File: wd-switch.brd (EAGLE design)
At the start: 40.3 x 59.7 mm, 18 parts, among them Q1 BC337, Q3 IRL540N, Q4 IRL540N, X1 KUSBVX

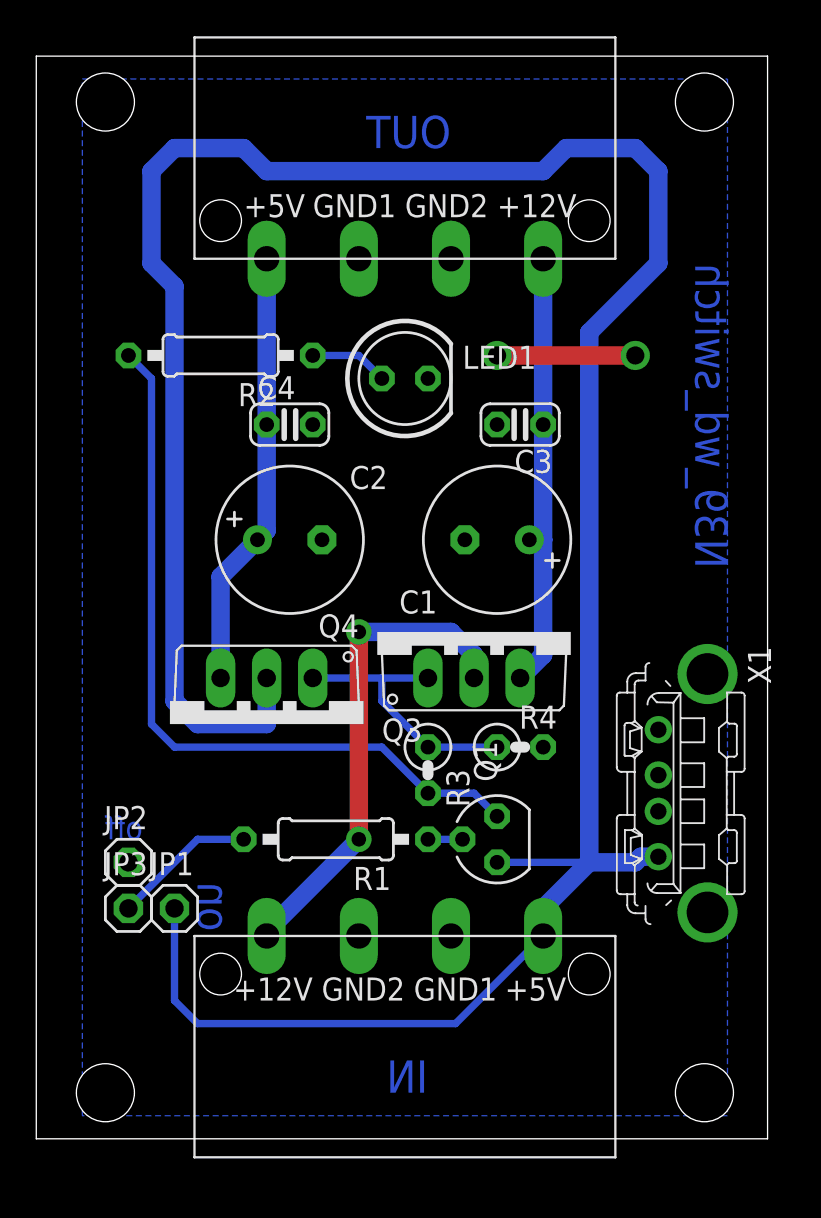
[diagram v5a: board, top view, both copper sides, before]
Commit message: WD-Switch jetzt mit Relais
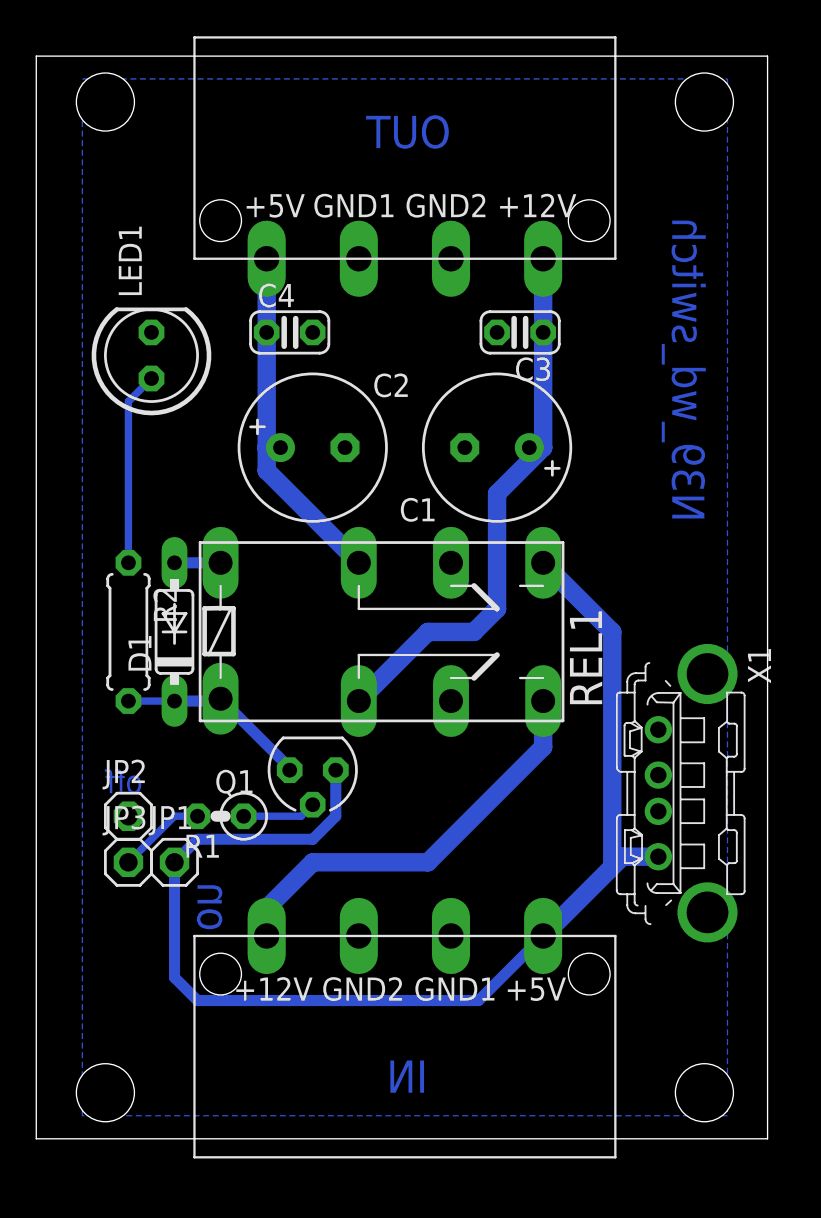
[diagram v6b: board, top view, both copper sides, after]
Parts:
- removed Q3, Q4: IRL540N, n39:TO220V
- removed R3: 100R, resistor:0207/2V
- removed R4: 100K, resistor:0207/2V
- added D1: 1N4148DO35-7, diode:DO35-7
- added REL1: RELAIS_2_WECHSLER, n39:RELAIS_DIL_M4
- R1: device resistor:0207/10 -> resistor:0207/2V
- R2: device resistor:0207/10 -> resistor:0207/7
- moved R2 16.1 mm to (5.08, 27.9), turned to 270 degrees
- moved LED1 14.0 mm to (6.35, 43.2), turned to 90 degrees
- moved Q1 10.9 mm to (15.2, 20.3), turned to 180 degrees
- moved R1 6.48 mm to (10.2, 17.8)
- moved C2 5.24 mm to (15.2, 38.1)
- moved C3 5.08 mm to (26.7, 44.5)
- moved C4 5.08 mm to (14.0, 44.5)
- moved C1 5.08 mm to (25.4, 38.1)
- moved JP1 2.54 mm to (7.62, 15.2)
- moved JP2 2.54 mm to (5.08, 17.8)
- moved JP3 2.54 mm to (5.08, 15.2)
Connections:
- removed net N$1: Q3.1, Q4.1, R3.1, R4.1
- net GND: now also D1.A, REL1.2; no longer R4.2
- net N$11: now also D1.C, REL1.1; no longer R3.2
- net N$2: now also REL1.P0; no longer Q3.3
- net N$4: now also REL1.P1; no longer Q4.3
- net VCC: now also REL1.S1; no longer Q4.2
- net VDD: now also REL1.S0; no longer Q3.2
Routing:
- net VCC: track 149.7 -> 67.4 mm
- net N$11: track 42.0 -> 10.6 mm
- net N$1: track 15.0 -> 0.00 mm
- net N$2: track 24.4 -> 30.8 mm
- net N$7: track 4.34 -> 10.7 mm
- net GND: track 7.62 -> 2.54 mm, vias 2 -> 0
- net N$4: track 24.2 -> 19.6 mm
- net VDD: track 27.0 -> 23.0 mm, vias 2 -> 0
- net N$5: track 7.93 -> 4.86 mm
- net N$3: track 1.91 -> 4.07 mm

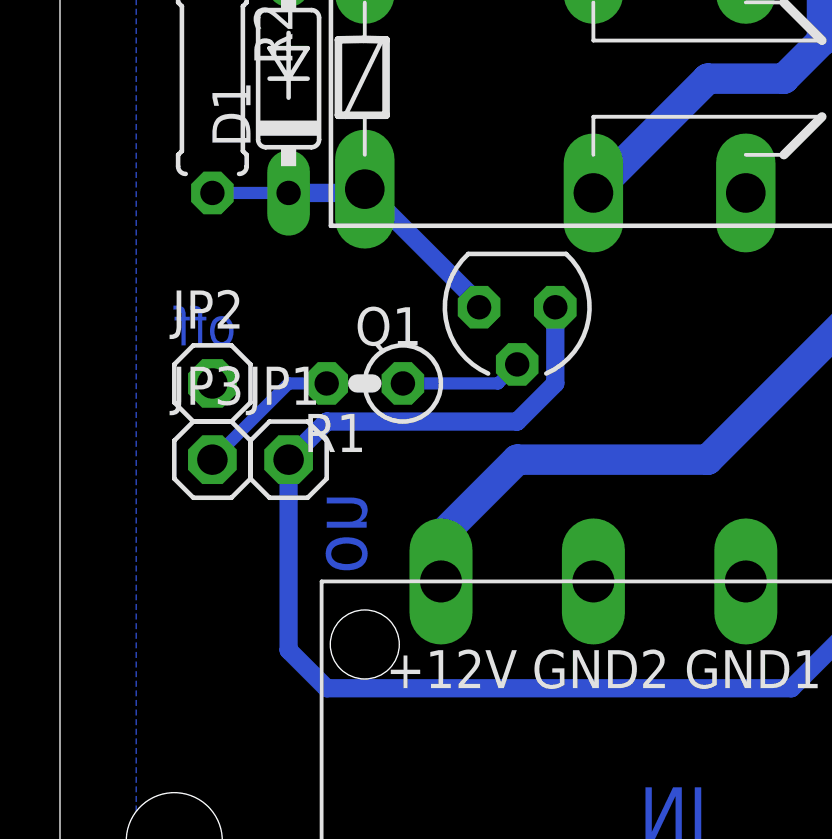
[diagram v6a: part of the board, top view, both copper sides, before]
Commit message: kleine Layoutanpassung, um GND-Durchlass zu verbreitern
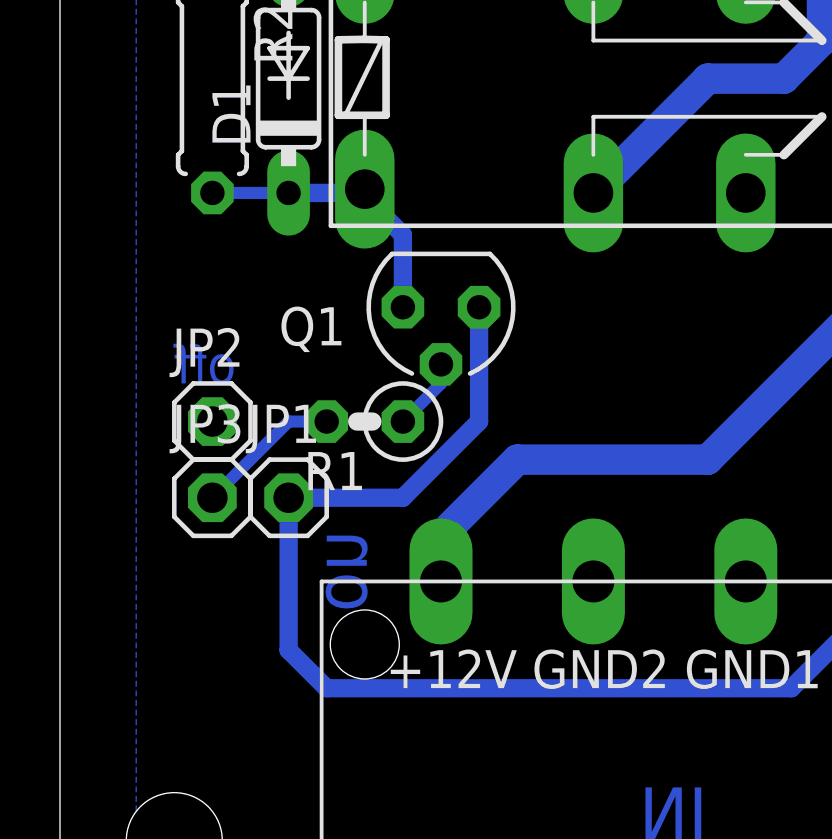
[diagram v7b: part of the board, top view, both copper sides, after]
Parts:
- moved Q1 2.54 mm to (12.7, 20.3)
- moved JP1 1.27 mm to (7.62, 14.0)
- moved JP2 1.27 mm to (5.08, 16.5)
- moved JP3 1.27 mm to (5.08, 14.0)
- moved R1 1.27 mm to (10.2, 16.5)
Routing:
- net VCC: track 67.4 -> 64.9 mm
- net N$3: track 4.07 -> 2.43 mm
- net N$11: track 10.6 -> 9.52 mm
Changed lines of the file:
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@@
 <text x="22.86" y="54.61" size="1.778" layer="16" font="vector" rot="MR0">OUT</text>
 <text x="36.83" y="50.8" size="1.778" layer="16" font="vector" rot="MR270">N39_wd_switch</text>
-<text x="3.81" y="20.32" size="1.27" layer="16" font="vector" rot="MR180">off</text>
-<text x="8.89" y="11.43" size="1.778" layer="16" font="vector" rot="MR90">on</text>
+<text x="3.81" y="19.05" size="1.27" layer="16" font="vector" rot="MR180">off</text>
+<text x="8.89" y="10.16" size="1.778" layer="16" font="vector" rot="MR90">on</text>
 </plain>
 <attributes>
@@
 <elements>
 <element name="IN" library="n39" package="PSW_5" value="" x="20.32" y="5.08" rot="R180"/>
-<element name="Q1" library="transistor-small-signal" package="SOT54A" value="BC337" x="15.24" y="20.32" rot="R180"/>
+<element name="Q1" library="transistor-small-signal" package="SOT54A" value="BC337" x="12.7" y="20.32" rot="R180"/>
 <element name="OUT" library="n39" package="PSW_5" value="" x="20.32" y="54.61"/>
-<element name="R1" library="resistor" package="0207/2V" value="150R" x="10.16" y="17.78" rot="R180"/>
+<element name="R1" library="resistor" package="0207/2V" value="150R" x="10.16" y="16.51" rot="R180"/>
 <element name="LED1" library="led" package="LED5MM" value="GN" x="6.35" y="43.18" rot="R90"/>
 <element name="R2" library="resistor" package="0207/7" value="150R" x="5.08" y="27.94" rot="R270"/>
@@
 <element name="C3" library="resistor" package="C025-024X044" value="100n" x="26.67" y="44.45" rot="R180"/>
 <element name="C4" library="resistor" package="C025-024X044" value="100n" x="13.97" y="44.45"/>
-<element name="JP1" library="pinhead" package="1X01" value="ON" x="7.62" y="15.24"/>
-<element name="JP2" library="pinhead" package="1X01" value="OFF" x="5.08" y="17.78"/>
-<element name="JP3" library="pinhead" package="1X01" value="IN" x="5.08" y="15.24"/>
+<element name="JP1" library="pinhead" package="1X01" value="ON" x="7.62" y="13.97"/>
+<element name="JP2" library="pinhead" package="1X01" value="OFF" x="5.08" y="16.51"/>
+<element name="JP3" library="pinhead" package="1X01" value="IN" x="5.08" y="13.97"/>
 <element name="X1" library="con-kycon" package="KUSBVX" value="KUSBVX" x="34.29" y="19.05" rot="R270"/>
 <element name="REL1" library="n39" package="RELAIS_DIL_M4" value="RELAIS_2_WECHSLER" x="17.78" y="26.67"/>
@@
 <contactref element="Q1" pad="C"/>
 <contactref element="JP1" pad="1"/>
-<wire x1="7.62" y1="15.24" x2="7.62" y2="8.89" width="0.6096" layer="16"/>
+<wire x1="7.62" y1="13.97" x2="7.62" y2="8.89" width="0.6096" layer="16"/>
 <wire x1="7.62" y1="8.89" x2="8.89" y2="7.62" width="0.6096" layer="16"/>
 <wire x1="8.89" y1="7.62" x2="24.38" y2="7.62" width="0.6096" layer="16"/>
@@
 <wire x1="27.94" y1="31.75" x2="31.75" y2="27.94" width="1.016" layer="16"/>
 <wire x1="31.75" y1="27.94" x2="31.75" y2="15.24" width="1.016" layer="16"/>
-<wire x1="15.24" y1="16.51" x2="16.51" y2="17.78" width="0.6096" layer="16"/>
-<wire x1="16.51" y1="17.78" x2="16.51" y2="20.32" width="0.6096" layer="16"/>
-<wire x1="7.62" y1="15.24" x2="8.89" y2="16.51" width="0.6096" layer="16"/>
-<wire x1="8.89" y1="16.51" x2="15.24" y2="16.51" width="0.6096" layer="16"/>
+<wire x1="7.62" y1="13.97" x2="11.43" y2="13.97" width="0.6096" layer="16"/>
+<wire x1="11.43" y1="13.97" x2="13.97" y2="16.51" width="0.6096" layer="16"/>
+<wire x1="13.97" y1="16.51" x2="13.97" y2="20.32" width="0.6096" layer="16"/>
 <wire x1="32.31" y1="15.55" x2="31.75" y2="15.24" width="0" layer="19" extent="16-16"/>
 </signal>
@@
 </signal>
 <signal name="N$3">
+<contactref element="Q1" pad="B"/>
 <contactref element="R1" pad="1"/>
-<contactref element="Q1" pad="B"/>
-<wire x1="11.43" y1="17.78" x2="14.605" y2="17.78" width="0.4064" layer="16"/>
-<wire x1="14.605" y1="17.78" x2="15.24" y2="18.415" width="0.4064" layer="16"/>
+<wire x1="11.43" y1="16.51" x2="12.7" y2="17.78" width="0.4064" layer="16"/>
+<wire x1="12.7" y1="17.78" x2="12.7" y2="18.415" width="0.4064" layer="16"/>
 </signal>
 <signal name="N$8">
@@
 <wire x1="5.08" y1="31.75" x2="5.08" y2="40.64" width="0.4064" layer="16"/>
 <wire x1="5.08" y1="40.64" x2="6.35" y2="41.91" width="0.4064" layer="16"/>
-</signal>
-<signal name="N$5">
-<contactref element="R1" pad="2"/>
-<contactref element="JP3" pad="1"/>
-<wire x1="5.08" y1="15.24" x2="7.62" y2="17.78" width="0.4064" layer="16"/>
-<wire x1="7.62" y1="17.78" x2="8.89" y2="17.78" width="0.4064" layer="16"/>
 </signal>
 <signal name="N$6">
@@
 <wire x1="7.62" y1="24.13" x2="10.033" y2="24.13" width="0.6096" layer="16"/>
 <wire x1="10.033" y1="24.13" x2="10.16" y2="24.257" width="0.4064" layer="16"/>
-<wire x1="13.97" y1="20.32" x2="13.97" y2="20.447" width="0.4064" layer="16"/>
-<wire x1="13.97" y1="20.447" x2="10.16" y2="24.257" width="0.6096" layer="16"/>
 <wire x1="7.62" y1="24.13" x2="5.08" y2="24.13" width="0.4064" layer="16"/>
+<wire x1="10.033" y1="24.13" x2="11.43" y2="22.733" width="0.6096" layer="16"/>
+<wire x1="11.43" y1="22.733" x2="11.43" y2="20.32" width="0.6096" layer="16"/>
+</signal>
+<signal name="N$1">
+<contactref element="R1" pad="2"/>
+<contactref element="JP3" pad="1"/>
+<wire x1="5.08" y1="13.97" x2="7.62" y2="16.51" width="0.4064" layer="16"/>
+<wire x1="7.62" y1="16.51" x2="8.89" y2="16.51" width="0.4064" layer="16"/>
 </signal>
 </signals>
